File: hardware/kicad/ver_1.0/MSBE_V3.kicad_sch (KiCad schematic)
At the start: 145 parts, among them J1 USB_C_Receptacle_USB2.0_16P, J10 Low-V, J2 USB_C_Receptacle_USB2.0_16P, J3 Touch Pads, J4 Touch Pads, J5 UART, J6 UART, J7 Prog, J8 Prog, J9 High-V, U1 NPM1100-CAAA-R7, U10 MAX98357AEWL_T, U2 NPM1100-CAAA-R7, U3 NRF5340-CLAA-R, U4 NRF5340-CLAA-R, U5 BMA400, U6 BMA400, U7 MPR121QR2, U8 MPR121QR2, U9 MAX98357AEWL_T, Y1 Crystal, Y2 Crystal

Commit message: updated all
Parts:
- U3, U4: footprint myLib:NRF5340-CLAA-R -> myLib:NRF5340
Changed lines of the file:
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@@
 			)
 		)
-		(property "Footprint" "myLib:NRF5340-CLAA-R"
+		(property "Footprint" "myLib:NRF5340"
 			(at 151.13 100.965 0)
 			(effects
@@
 			)
 		)
-		(property "Footprint" "myLib:NRF5340-CLAA-R"
+		(property "Footprint" "myLib:NRF5340"
 			(at 462.915 99.695 0)
 			(effects

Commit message: new stuff added
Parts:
- removed BT1: Battery_Cell, myLib:Pad_2Pin_1.5x0.8mm, symbol Device:Battery_Cell
- removed C1, C33, C37: 4.7uF, Capacitor_SMD:C_0603_1608Metric, symbol Device:C
- removed C11, C12: 12pF, Capacitor_SMD:C_0603_1608Metric, symbol Device:C
- removed C15, C21, C29, C31, C45: 1.0uF, Capacitor_SMD:C_0603_1608Metric, symbol Device:C
- removed C17, C19, C25, C27, C43, C47, C49, C51, C55, C57: 100nF, Capacitor_SMD:C_0603_1608Metric, symbol Device:C
- removed C23: 2.2nF, Capacitor_SMD:C_0603_1608Metric, symbol Device:C
- removed C3, C5, C64, C7, C70: 10uF, Capacitor_SMD:C_0603_1608Metric, symbol Device:C
- removed C35, C39: N.C., Capacitor_SMD:C_0603_1608Metric, symbol Device:C
- removed C40: 0.7pF, Capacitor_SMD:C_0603_1608Metric, symbol Device:C
- removed C53, C59, C63, C69, C9: 0.1uF, Capacitor_SMD:C_0603_1608Metric, symbol Device:C
- removed C61, C62, C66, C67, C68: 30pF, Capacitor_SMD:C_0603_1608Metric, symbol Device:C
- removed C65, C71: 47uF, Capacitor_SMD:C_0603_1608Metric, symbol Device:C
- removed D1, D3: LED, LED_SMD:LED_0603_1608Metric, symbol Device:LED
- removed J1: USB_C_Receptacle_USB2.0_16P, Connector_USB:USB_C_Receptacle_GCT_USB4110, symbol Connector:USB_C_Receptacle_USB2.0_16P
- removed J10: Low-V, myLib:Pad_prog_4Pad, symbol Connector:Conn_01x05_Pin
- removed J3: Touch Pads, myLib:Pad_1Pin_2x1.2mm, symbol Connector:Conn_01x03_Pin
- removed J5: UART, myLib:Pad_3Pin_1.5x0.8mm, symbol Connector:Conn_01x03_Pin
- removed J7: Prog, myLib:Pad_prog_4Pad, symbol Connector:Conn_01x05_Pin
- removed J9: High-V, myLib:Pad_prog_4Pad, symbol Connector:Conn_01x05_Pin
- removed L1: 2.2uH, Inductor_SMD:L_0603_1608Metric, symbol Device:L
- removed L3, L5: 10uH, Inductor_SMD:L_0603_1608Metric, symbol Device:L
- removed L7: 2.2nH, Inductor_SMD:L_0603_1608Metric, symbol Device:L
- removed LS1: SPH18R1LM4H-1-8, myLib:MIC_SPH18R1LM4H_KNO, symbol mySch_lib:SPH18R1LM4H-1-8
- removed LS3, LS4, LS5, LS6: Boneconduction, myLib:Pad_2Pin_1.5x0.8mm, symbol Device:Speaker
- removed R1, R3: 1K5R, Resistor_SMD:R_0603_1608Metric, symbol Device:R
- removed R11, R5, R9: 5K1R, Resistor_SMD:R_0603_1608Metric, symbol Device:R
- removed R13, R15: 4.7k, Resistor_SMD:R_0603_1608Metric, symbol Device:R
- removed R17: 2R2, Resistor_SMD:R_0603_1608Metric, symbol Device:R
- removed R19: 75k, Resistor_SMD:R_0603_1608Metric, symbol Device:R
- removed R21, R22, R25, R28, R29: 1K5, Resistor_SMD:R_0603_1608Metric, symbol Device:R
- removed R23, R24, R26, R30, R31: 1K8, Resistor_SMD:R_0603_1608Metric, symbol Device:R
- removed R27, R32: N.C., Resistor_SMD:R_0603_1608Metric, symbol Device:R
- removed R7: 10K, Resistor_SMD:R_0603_1608Metric, symbol Device:R
- removed U1: NPM1100-CAAA-R7, myLib:NPM1100-CAAA-BGA25C40P5X5_207X207X52N, symbol mySch_lib:NPM1100-CAAA-R7
- removed U10, U9: MAX98357AEWL_T, myLib:MAX98357A_BGA9N40P3X3_134X143X69N, symbol mySch_lib:MAX98357AEWL_T
- removed U3: NRF5340-CLAA-R, myLib:NRF5340, symbol mySch_lib:NRF5340-CLAA-R
- removed U5: BMA400, myLib:QFN_BMA400_BOS, symbol mySch_lib:BMA400
- removed U7: MPR121QR2, myLib:MPR121, symbol mySch_lib:MPR121QR2
- Y1: value Crystal -> 32.768kHz
- Y2: value Crystal -> 32MHz
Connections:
- net AVSS: now also U4.G11 (P0.02/NFC1), U4.H12 (P0.03/NFC2)
- net X2: now reaches Y1.1
- net X2: now also U4.F12 (P0.01/XL2)
- net X1: now reaches Y1.2
- net X1: now also U4.F11 (P0.00/XL1)
- no-connect marks 24 -> 12
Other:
- added sheet test (untitled.kicad_sch)
- note removed: "12db gain connected to GND 15db gain connected with 100kohm 9db gain leave open"
- note removed: "LEFT CHANNEL SELECTED"
- note removed: "Logic Level Shifter Programing"
- note removed: "RIGHT CHANNEL SELECTED"
- note removed: "Right"
- note removed: "Speaker & Amplifier"
- moved on the sheet: BT2, C10, C13, C14, C16, C18, C2, C20, C22, C24, C26, C28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

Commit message: modified schematic only
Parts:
- removed C36: N.C., Capacitor_SMD:C_0603_1608Metric, symbol Device:C
- added AE1, AE2: Antenna_Shield, RF_Antenna:Texas_SWRA117D_2.4GHz_Left, symbol Device:Antenna_Shield
- added BT2: Battery_Cell, mylib:Pad_3Pin_1.5x0.8mm, symbol Device:Battery_Cell
- added C10, C54, C60, C63, C69: 0.1uF, Capacitor_SMD:C_0603_1608Metric, symbol Device:C
- added C13, C14: 12pF, Capacitor_SMD:C_0603_1608Metric, symbol Device:C
- added C17, C22, C31, C32, C46: 1.0uF, Capacitor_SMD:C_0603_1608Metric, symbol Device:C
- added C19, C20, C27, C28, C44, C48, C51, C52, C56, C58: 100nF, Capacitor_SMD:C_0603_1608Metric, symbol Device:C
- added C2, C35, C40: 4.7uF, Capacitor_SMD:C_0603_1608Metric, symbol Device:C
- added C24: 2.2nF, Capacitor_SMD:C_0603_1608Metric, symbol Device:C
- added C4, C6, C64, C70, C8: 10uF, Capacitor_SMD:C_0603_1608Metric, symbol Device:C
- added C42: N.C., Capacitor_SMD:C_0603_1608Metric, symbol Device:C
- added C43: 0.7pF, Capacitor_SMD:C_0603_1608Metric, symbol Device:C
- added C61, C62, C66, C67, C68: 30pF, Capacitor_SMD:C_0603_1608Metric, symbol Device:C
- added C65, C71: 47uF, Capacitor_SMD:C_0603_1608Metric, symbol Device:C
- added D3, D4: LED, LED_SMD:LED_0603_1608Metric, symbol Device:LED
- added J10: Low-V, mylib:Pad_prog_4Pad, symbol Connector:Conn_01x05_Pin
- added J2: USB_C_Receptacle_USB2.0_16P, Connector_USB:USB_C_Receptacle_GCT_USB4110, symbol Connector:USB_C_Receptacle_USB2.0_16P
- added J4: Touch Pads, mylib:Pad_3Pin_1.5x0.8mm, symbol Connector:Conn_01x03_Pin
- added J7: UART, mylib:Pad_3Pin_1.5x0.8mm, symbol Connector:Conn_01x03_Pin
- added J8: Prog, mylib:Pad_prog_4Pad, symbol Connector:Conn_01x05_Pin
- added J9: High-V, mylib:Pad_prog_4Pad, symbol Connector:Conn_01x05_Pin
- added L2: 2.2uH, Inductor_SMD:L_0603_1608Metric, symbol Device:L
- added L4, L6: 10uH, Inductor_SMD:L_0603_1608Metric, symbol Device:L
- added L8: 2.2nH, Inductor_SMD:L_0603_1608Metric, symbol Device:L
- added LS2: SPH18R1LM4H-1-8, mylib:MIC_SPH18R1LM4H_KNO, symbol mySch_lib:SPH18R1LM4H-1-8
- added LS3, LS4, LS5, LS6: Boneconduction, mylib:Pad_2Pin_1.5x0.8mm, symbol Device:Speaker
- added R11, R12, R7: 5K1R, Resistor_SMD:R_0603_1608Metric, symbol Device:R
- added R15, R16: 4.7k, Resistor_SMD:R_0603_1608Metric, symbol Device:R
- added R18: 2R2, Resistor_SMD:R_0603_1608Metric, symbol Device:R
- added R20: 75k, Resistor_SMD:R_0603_1608Metric, symbol Device:R
- added R21, R22, R25, R28, R29: 1K5, Resistor_SMD:R_0603_1608Metric, symbol Device:R
- added R23, R24, R26, R30, R31: 1K8, Resistor_SMD:R_0603_1608Metric, symbol Device:R
- added R27, R32: N.C., Resistor_SMD:R_0603_1608Metric, symbol Device:R
- added R3, R4: 1K5R, Resistor_SMD:R_0603_1608Metric, symbol Device:R
- added R8: 10K, Resistor_SMD:R_0603_1608Metric, symbol Device:R
- added U10, U9: MAX98357AEWL_T, mylib:MAX98357A_BGA9N40P3X3_134X143X69N, symbol mySch_lib:MAX98357AEWL_T
- added U2: NPM1100-CAAA-R7, mylib:NPM1100-CAAA-BGA25C40P5X5_207X207X52N, symbol mySch_lib:NPM1100-CAAA-R7
- added U4: NRF5340-CLAA-R, mylib:NRF5340-CLAA-R, symbol mySch_lib:NRF5340-CLAA-R
- added U6: BMA400, mylib:QFN_BMA400_BOS, symbol mySch_lib:BMA400
- added U8: MPR121QR2, mylib:MPR121, symbol mySch_lib:MPR121QR2
- added Y2: Crystal, mylib:Crystal_24MHz-ECS-240-12-37B-CKY-TR, symbol Device:Crystal
- added Y4: 32.768kHz, mylib:Crystal_24MHz-ECS-240-12-37B-CKY-TR, symbol Device:Crystal
- BT1: renamed from BT2; footprint myLib:Pad_2Pin_1.5x0.8mm -> mylib:Pad_3Pin_1.5x0.8mm
- J3: renamed from J4; footprint myLib:Pad_1Pin_2x1.2mm -> mylib:Pad_3Pin_1.5x0.8mm
- J5: renamed from J6; footprint myLib:Pad_3Pin_1.5x0.8mm -> mylib:Pad_3Pin_1.5x0.8mm
- J6: renamed from J8; footprint myLib:Pad_prog_4Pad -> mylib:Pad_prog_4Pad
- LS1: renamed from LS2; footprint myLib:MIC_SPH18R1LM4H_KNO -> mylib:MIC_SPH18R1LM4H_KNO
- U1: renamed from U2; footprint myLib:NPM1100-CAAA-BGA25C40P5X5_207X207X52N -> mylib:NPM1100-CAAA-BGA25C40P5X5_207X207X52N
- U3: renamed from U4; footprint myLib:NRF5340 -> mylib:NRF5340-CLAA-R
- U5: renamed from U6; footprint myLib:QFN_BMA400_BOS -> mylib:QFN_BMA400_BOS
- U7: renamed from U8; footprint myLib:MPR121 -> mylib:MPR121
- Y1: renamed from Y2; footprint myLib:Crystal_24MHz-ECS-240-12-37B-CKY-TR -> mylib:Crystal_24MHz-ECS-240-12-37B-CKY-TR
- Y3: renamed from Y1; footprint myLib:Crystal_24MHz-ECS-240-12-37B-CKY-TR -> mylib:Crystal_24MHz-ECS-240-12-37B-CKY-TR
- renumbered C2 to C1, C13 to C11, C14 to C12, C16 to C15, C18 to C16, C20 to C18, C22 to C21, C24 to C23, C26 to C25, C28 to C26, C30 to C29, C4 to C3, C32 to C30, C34 to C33, C38 to C36, C41 to C38, C42 to C39, C44 to C41, C46 to C45, C48 to C47, C50 to C49, C6 to C5, C52 to C50, C54 to C53, C56 to C55, C58 to C57, C60 to C59, C8 to C7, C10 to C9, D2 to D1, D4 to D2, J2 to J1, L2 to L1, L4 to L3, L6 to L5, L8 to L7, R2 to R1, R12 to R10, R14 to R13, R16 to R14, R18 to R17, R20 to R19, R4 to R2, R6 to R5, R8 to R6, R10 to R9
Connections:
- net +3.3V: now also BT2.1 (+), C2.2, C63.1, C64.1, C65.1, C69.1, C70.1, C71.1, U10.A2 (VDD), U2.D1 (VBAT), U2.D2 (VBAT), U9.A2 (VDD)
- net AVSS: now also AE1.2 (Shield), AE2.2 (Shield), BT2.2 (-), C10.2, C13.2, C14.2, C17.2, C19.1, C2.1, C20.1, C22.1, C24.1, C27.1, C28.1, C31.1, C32.2, C35.2, C4.1, C40.2, C42.2, C43.2, C44.1, C46.2, C48.1, C51.2, C52.1, C54.1, C56.1, C58.2, C6.1, C60.2, C63.2, C64.2, C65.2, C69.2, C70.2, C71.2, C8.1, J2.A1 (GND), J2.A12 (GND), J2.B1 (GND), J2.B12 (GND), J2.S1 (SHIELD), J7.3 (Pin_3), J8.4 (Pin_4), LS2.3 (GROUND), R11.1, R12.1, R20.2, R27.1, R32.1, R7.1, R8.1, U10.C2 (GND), U2.A5 (PVSS), U2.B3 (VOUTBSET1), U2.B4 (VOUTBSET0), U2.C4 (AVSS), U2.C5 (AVSS), U2.D3 (SHPHLD), U2.D4 (SHPACT), U2.E5 (MODE), U4.A5 (VSS), U4.B2 (VSS), U4.B9 (VSS), U4.C2 (VSS), U4.D12 (VSS), U4.E5 (VSS), U4.E6 (VSS), U4.E7 (VSS), U4.E8 (VSS), U4.F5 (VSS), U4.F6 (VSS), U4.F7 (VSS), U4.F8 (VSS), U4.G11 (P0.02/NFC1), U4.G5 (AVSS), U4.G6 (VSS), U4.G7 (VSS), U4.G8 (VSS), U4.H12 (P0.03/NFC2), U4.K6 (AVSS), U6.1 (SDO), U6.8 (GNDIO), U6.9 (GND), U8.4 (ADDR), U8.6 (VSS), U9.C2 (GND)
- net D+: now also J2.A6 (D+), J2.B6 (D+), U2.A2 (D+), U4.A12 (D+)
- net D-: now also J2.A7 (D-), J2.B7 (D-), U2.A1 (D-), U4.A11 (D-)
- net I2C_SCL: now also R15.2, U4.G10 (P0.04/AIN0), U6.12 (SCX), U8.2 (SCL)
- net I2C_SDA: now also R16.2, U4.F10 (P0.05/AIN1), U6.2 (SDX), U8.3 (SDA)
- net INT1: now also U4.H10 (P0.06/AIN2), U6.5 (INT1)
- net INT2: now also U4.J10 (P0.07/AIN3), U6.6 (INT2)
- net IRQ: now also U8.1 (*IRQ)
- net ISET: now also U2.D5 (ISET), U4.K4 (P0.22)
- net LRCLK: now also U10.C3 (LRCLK), U4.C8 (P1.13), U9.C3 (LRCLK)
- net MIC_CLOCK: now also LS2.4 (CLOCK), U4.J2 (P0.26/AIN5)
- net MIC_DATA: now also LS2.1 (DATA), U4.L1 (P0.25/AIN4)
- net RX: now also J7.2 (Pin_2)
- net SCK: now also U10.C1 (BCLK), U4.C7 (P1.12), U9.C1 (BCLK)
- net SDOUT: now also U10.B1 (DIN), U4.C9 (P1.14), U9.B1 (DIN)
- net SD_MODE: now also U10.A1 (SD_MODE), U4.K5 (P0.20), U9.A1 (SD_MODE)
- net SWDCLK: now also J8.3 (Pin_3), U4.F2 (SWDCLK)
- net SWDIO: now also J8.2 (Pin_2), U4.F1 (SWDIO)
- net TX: now also J7.1 (Pin_1)
- net VBUS: now also C4.2, J2.A4 (VBUS), J2.A9 (VBUS), J2.B4 (VBUS), J2.B9 (VBUS), R18.2, U2.B1 (VBUS), U2.B2 (VBUS)
- net VDD: now also C10.1, C32.1, C46.1, C51.1, C52.2, C58.1, C6.2, J8.1 (Pin_1), L2.1, LS2.5 (VDD), R15.1, R16.1, U2.B5 (VOUTB), U2.C3 (VTERMSET), U4.B10 (VDD), U4.B12 (VDDH), U4.B7 (VDD), U4.E11 (VDD), U6.10 (CSB), U6.3 (VDDIO), U6.7 (VDD), U8.20 (VDD)
- net VSYS: now also R3.2, R4.2, U2.C1 (VSYS), U2.C2 (VSYS)
- net X1: now also U4.F11 (P0.00/XL1), Y4.2
- net X2: now also U4.F12 (P0.01/XL2), Y4.1
- net nRESET: now also C54.2, J8.5 (Pin_5), U4.G2 (nRESET)
- net at C39.1, L7.2: now also U3.D1 (ANT)
- net RF: no longer names the net of C38.1, L7.1
- net RF: now also AE2.1 (A)
- new net: AE1.1 (A), C42.1, L8.1
- new net: R32.2, U10.B2 (GAIN_SLOT)
- new net: C60.1, U8.5 (VREG)
- new net: L2.2, U2.A4 (SW)
- new net: LS3.2, LS4.2, U9.A3 (OUTP)
- new net: R27.2, U9.B2 (GAIN_SLOT)
- new net: LS3.1, LS4.1, U9.B3 (OUTN)
- new net: C17.1, L4.2, U4.A7 (DECD)
- new net: C8.2, U2.A3 (DEC)
- new net: R8.2, U2.E1 (NTC)
- new net: C28.2, U4.B5 (DECN)
- new net: R29.2, R31.2
- new net: C40.1, R18.1, U4.B11 (VBUS)
- new net: C27.2, U4.H11 (VDD)
- new net: R25.2, R26.2
- new net: R21.2, R23.2
- new net: J4.3 (Pin_3), U8.10 (ELE2)
- new net: R20.1, U8.7 (REXT)
- new net: J4.1 (Pin_1), U8.8 (ELE0)
- new net: J4.2 (Pin_2), U8.9 (ELE1)
- new net: C44.2, U4.D2 (VDD)
- new net: J2.A5 (CC1), R11.2
- new net: R28.2, R30.2
- new net: C35.1, U4.C11 (DECUSB)
- new net: D4.1 (K), U2.E4 (CHG)
- new net: D4.2 (A), R4.1
- new net: C13.1, U4.A2 (XC2), Y2.1
- new net: LS5.1, LS6.1, U10.B3 (OUTN)
- new net: LS5.2, LS6.2, U10.A3 (OUTP)
- new net: C31.2, U4.B8 (DECA)
- new net: C22.2, C24.2, L6.2, U4.B1 (DECRF), U4.B4 (DECR)
- new net: D3.2 (A), R3.1
- new net: C43.1, L8.2, U4.D1 (ANT)
- new net: C14.1, U4.A1 (XC1), Y2.2
- new net: R22.2, R24.2
- new net: D3.1 (K), U2.E3 (ERR)
- new net: J2.B5 (CC2), R12.2
- new net: C48.2, U4.L5 (VDD)
- new net: R7.2, U2.E2 (ICHG)
- new net: L6.1, U4.B6 (DCC)
- new net: C20.2, U4.A3 (VDD)
- new net: L4.1, U4.A9 (DCCD)
- new net: C56.2, U4.K1 (VDD)
- new net: C19.2, U4.L11 (VDD)
- new net A1: C61.1, J9.1 (Pin_1), R21.1
- new net A2: C62.1, J9.2 (Pin_2), R22.1
- new net A3: C66.1, J9.3 (Pin_3), R25.1
- new net A4: C67.1, J9.4 (Pin_4), R28.1
- new net A5: C68.1, J9.5 (Pin_5), R29.1
- new net B1: C61.2, J10.1 (Pin_1), R23.1
- new net B2: C62.2, J10.2 (Pin_2), R24.1
- new net B3: C66.2, J10.3 (Pin_3), R26.1
- new net B4: C67.2, J10.4 (Pin_4), R30.1
- new net B5: C68.2, J10.5 (Pin_5), R31.1
- no-connect marks 12 -> 24
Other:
- removed sheet test
- note added: "12db gain connected to GND 15db gain connected with 100kohm 9db gain leave open"
- note added: "LEFT CHANNEL SELECTED"
- note added: "Logic Level Shifter Programing"
- note added: "RIGHT CHANNEL SELECTED"
- note added: "Right"
- note added: "Speaker & Amplifier"
- moved on the sheet: BT1, C1, C11, C12, C15, C16, C18, C21, C23, C25, C26, C29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

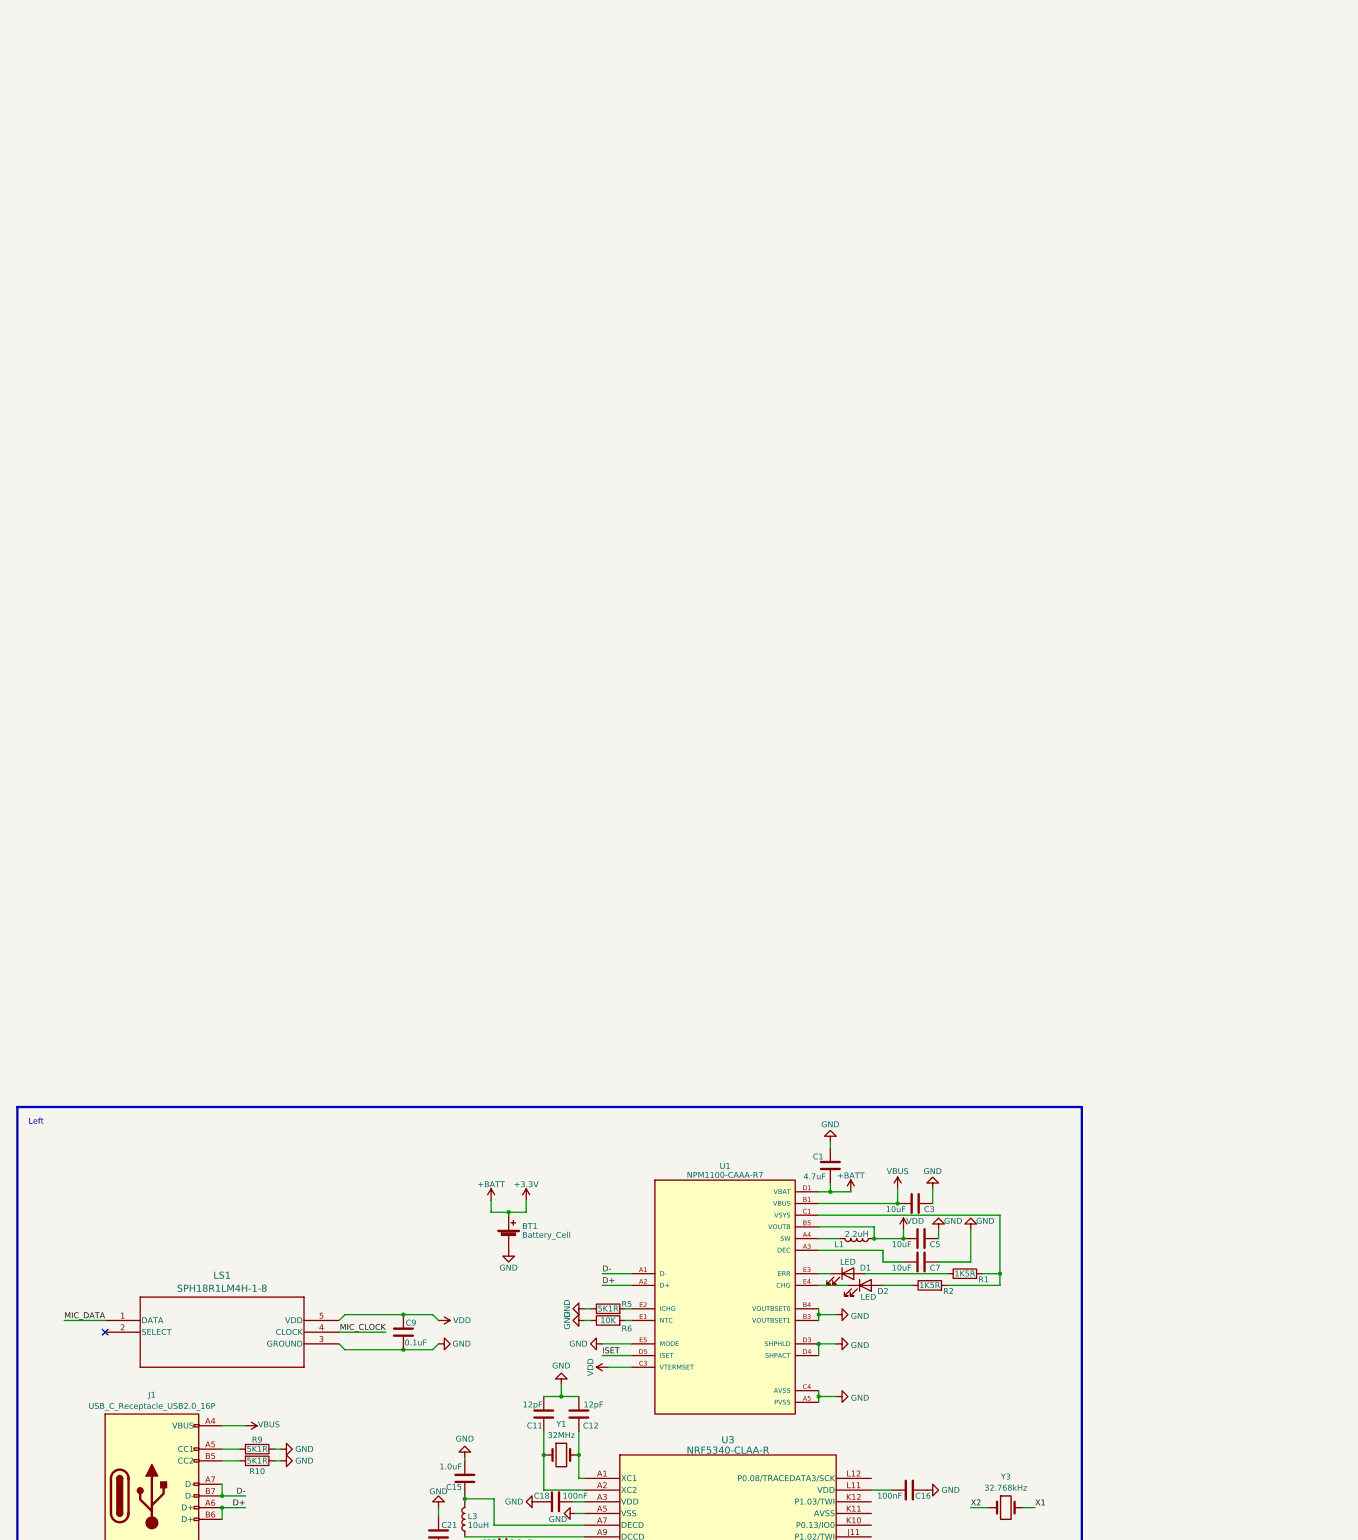
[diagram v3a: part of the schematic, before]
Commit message: new chip package
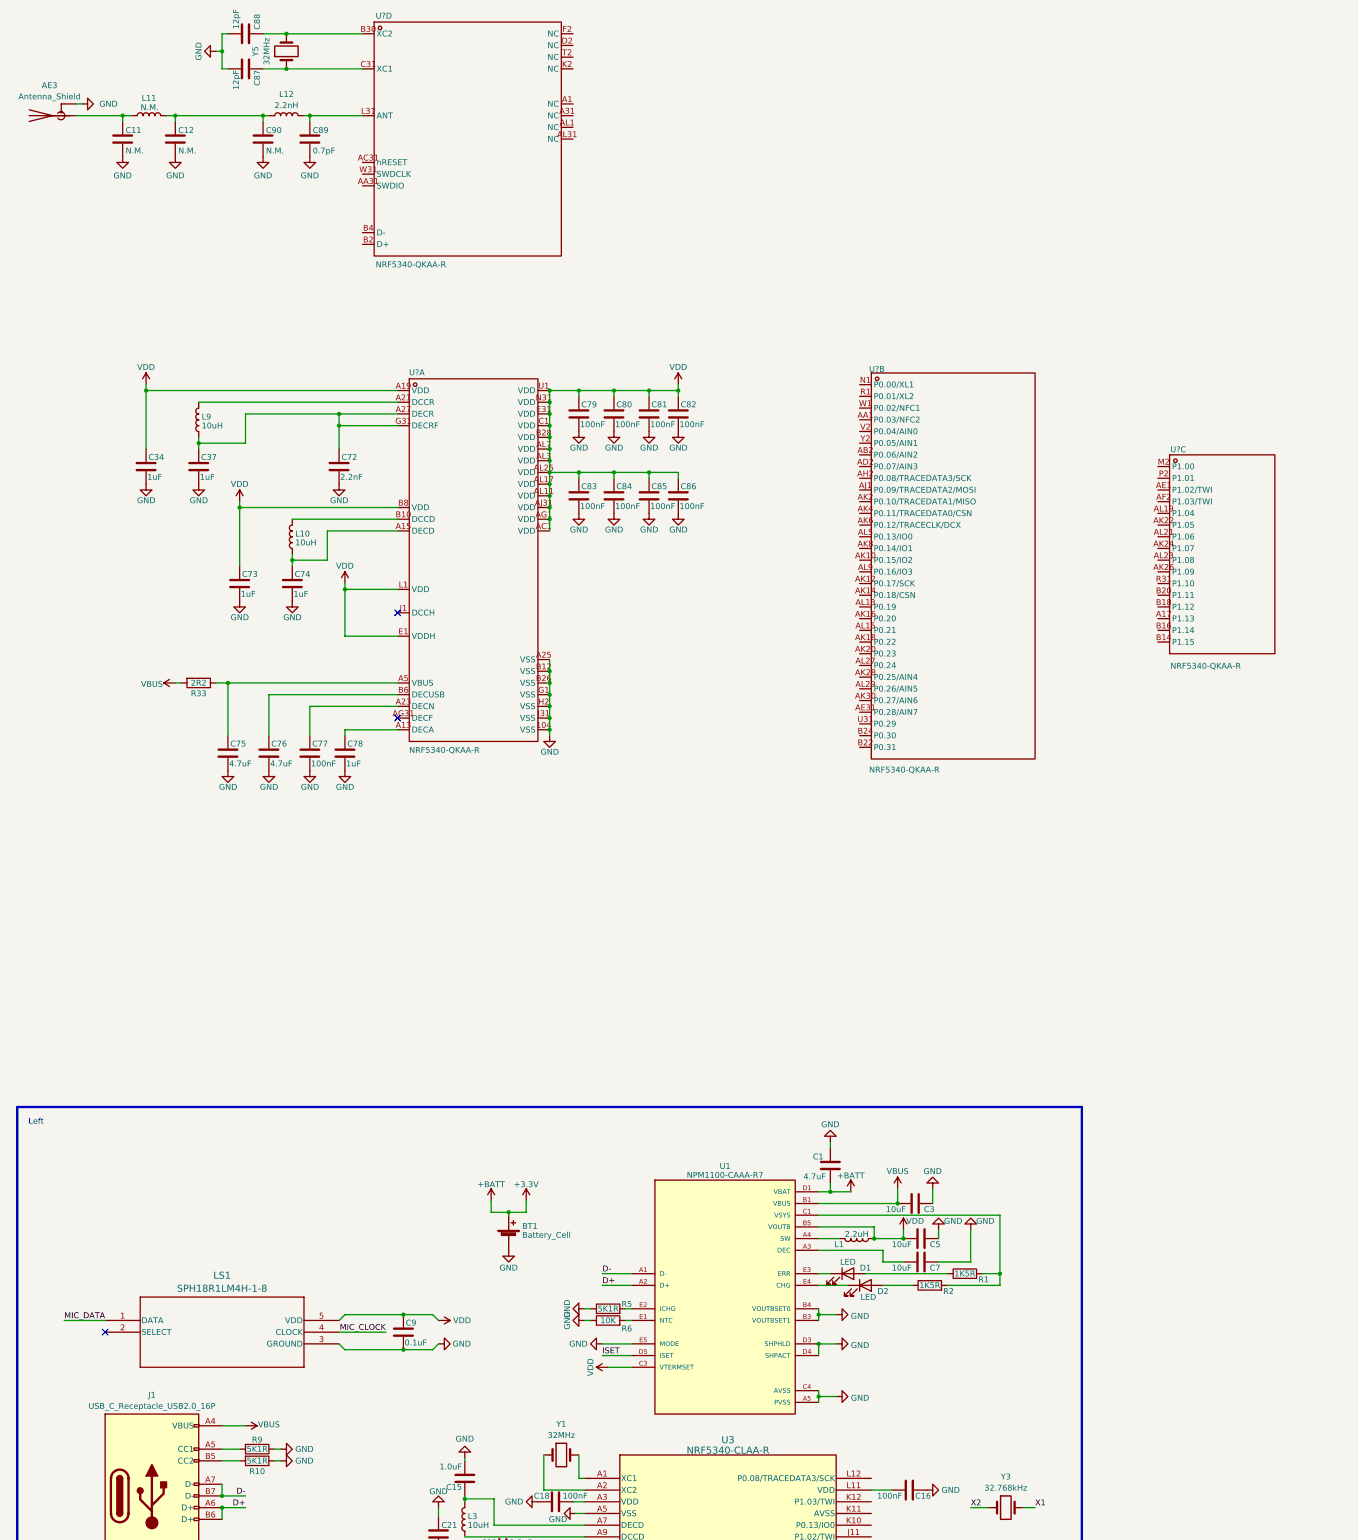
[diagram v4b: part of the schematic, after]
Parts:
- added AE3: Antenna_Shield, RF_Antenna:Texas_SWRA117D_2.4GHz_Left, symbol Device:Antenna_Shield
- added C34, C37, C73, C74, C78: 1uF, Capacitor_SMD:C_0603_1608Metric, symbol Device:C
- added C72: 2.2nF, Capacitor_SMD:C_0603_1608Metric, symbol Device:C
- added C75, C76: 4.7uF, Capacitor_SMD:C_0603_1608Metric, symbol Device:C
- added C77, C79, C80, C81, C82, C83, C84, C85, C86: 100nF, Capacitor_SMD:C_0603_1608Metric, symbol Device:C
- added C87, C88: 12pF, Capacitor_SMD:C_0603_1608Metric, symbol Device:C
- added C89: 0.7pF, Capacitor_SMD:C_0603_1608Metric, symbol Device:C
- added C90: N.M., Capacitor_SMD:C_0603_1608Metric, symbol Device:C
- added L10, L9: 10uH, Inductor_SMD:L_0603_1608Metric, symbol Device:L
- added L11: N.M., Inductor_SMD:L_0603_1608Metric, symbol Device:L
- added L12: 2.2nH, Inductor_SMD:L_0603_1608Metric, symbol Device:L
- added R33: 2R2, Resistor_SMD:R_0603_1608Metric, symbol Device:R
- added U? (x4): NRF5340-QKAA-R, AQFN-94_L7.0-W7.0-P0.40_NRF5340-QKAA-R, symbol 1_MSBE_V3-altium-import:root_0_NRF5340-QKAA-R_
- added Y5: 32MHz, mylib:Crystal_24MHz-ECS-240-12-37B-CKY-TR, symbol Device:Crystal
- C11, C12: value 12pF -> N.M.
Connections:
- net AVSS: now also AE3.2 (Shield), C34.2, C37.2, C72.2, C73.2, C74.2, C75.2, C76.2, C77.2, C78.2, C79.2, C80.2, C81.2, C82.2, C83.2, C84.2, C85.2, C86.2, C87.2, C88.2, C89.2, C90.2, U?.104 (VSS), U?.A25 (VSS), U?.B12 (VSS), U?.B26 (VSS), U?.G1 (VSS), U?.H2 (VSS), U?.J31 (VSS)
- net VBUS: now also R33.2
- net VDD: now also C34.1, C73.1, C79.1, C80.1, C81.1, C82.1, C83.1, C84.1, C85.1, C86.1, U?.A19 (VDD), U?.AC1 (VDD), U?.AG1 (VDD), U?.AJ31 (VDD), U?.AL11 (VDD), U?.AL17 (VDD), U?.AL25 (VDD), U?.AL3 (VDD), U?.AL7 (VDD), U?.B28 (VDD), U?.B8 (VDD), U?.C1 (VDD), U?.E1 (VDDH), U?.E31 (VDD), U?.L1 (VDD), U?.N31 (VDD), U?.U1 (VDD)
- net at U3.A1 (XC1), Y1.2: no longer C12.1
- net at U3.A2 (XC2), Y1.1: no longer C11.1
- new net: C37.1, C72.1, L9.1, U?.A27 (DECR), U?.G31 (DECRF)
- new net: C75.1, R33.1, U?.A5 (VBUS)
- new net: C74.1, L10.1, U?.A15 (DECD)
- new net: L10.2, U?.B10 (DCCD)
- new net: C88.1, U?.B30 (XC2), Y5.2
- new net: C12.1, C90.1, L11.2, L12.1
- new net: AE3.1 (A), C11.1, L11.1
- new net: C78.1, U?.A13 (DECA)
- new net: L9.2, U?.A21 (DCCR)
- new net: C76.1, U?.B6 (DECUSB)
- new net: C87.1, U?.C31 (XC1), Y5.1
- new net: C89.1, L12.2, U?.L31 (ANT)
- new net: C77.1, U?.A23 (DECN)
- no-connect marks 24 -> 26
